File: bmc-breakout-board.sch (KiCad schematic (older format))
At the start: 49 parts, among them J1 PinHeader_2x4, J10 PinHeader_2x4, J11 PinHeader_2x05, J12 61300411121, J13 0473460001, J14 PCIE_BUS_x1, J15 0473460001, J16 PinHeader_1x07, J17 UE27AC54100, J2 PinHeader_2x13, J3 PinHeader_2x08, J4 61300411121, J5 ME1016813401101, J6 61300411121, J7 DC_SOCKET, J8 PinHeader_2x05, J9 PinHeader_1x07, U1 FT234XD-R

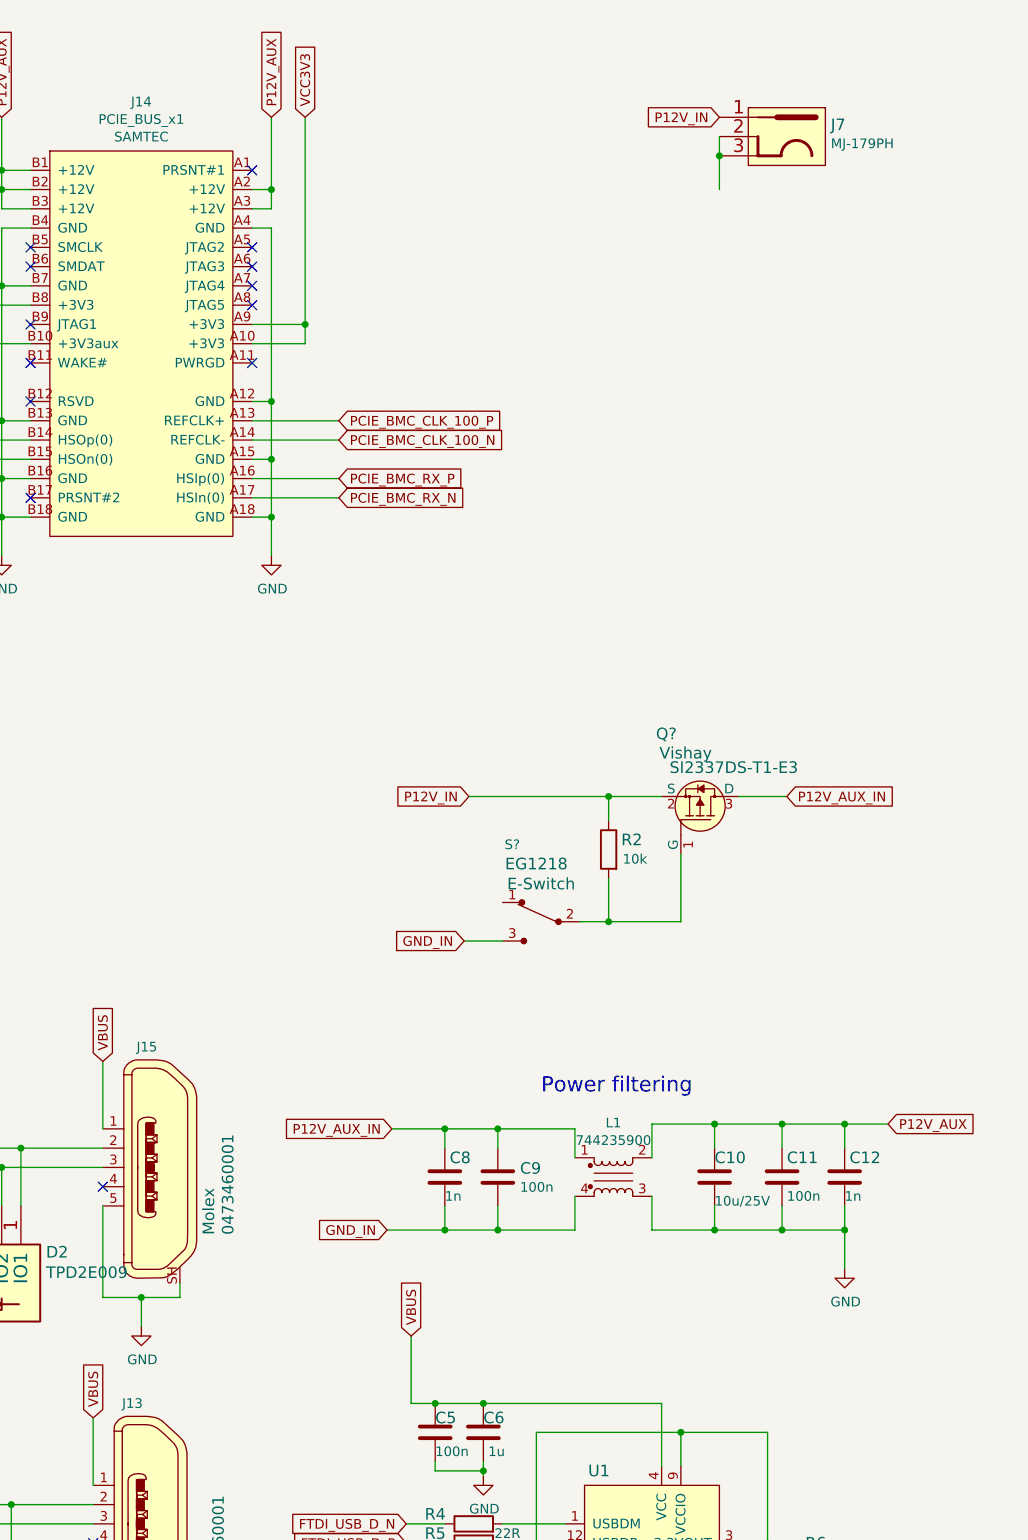
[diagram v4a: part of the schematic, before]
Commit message: Change signal assigment around the power filtering circuit
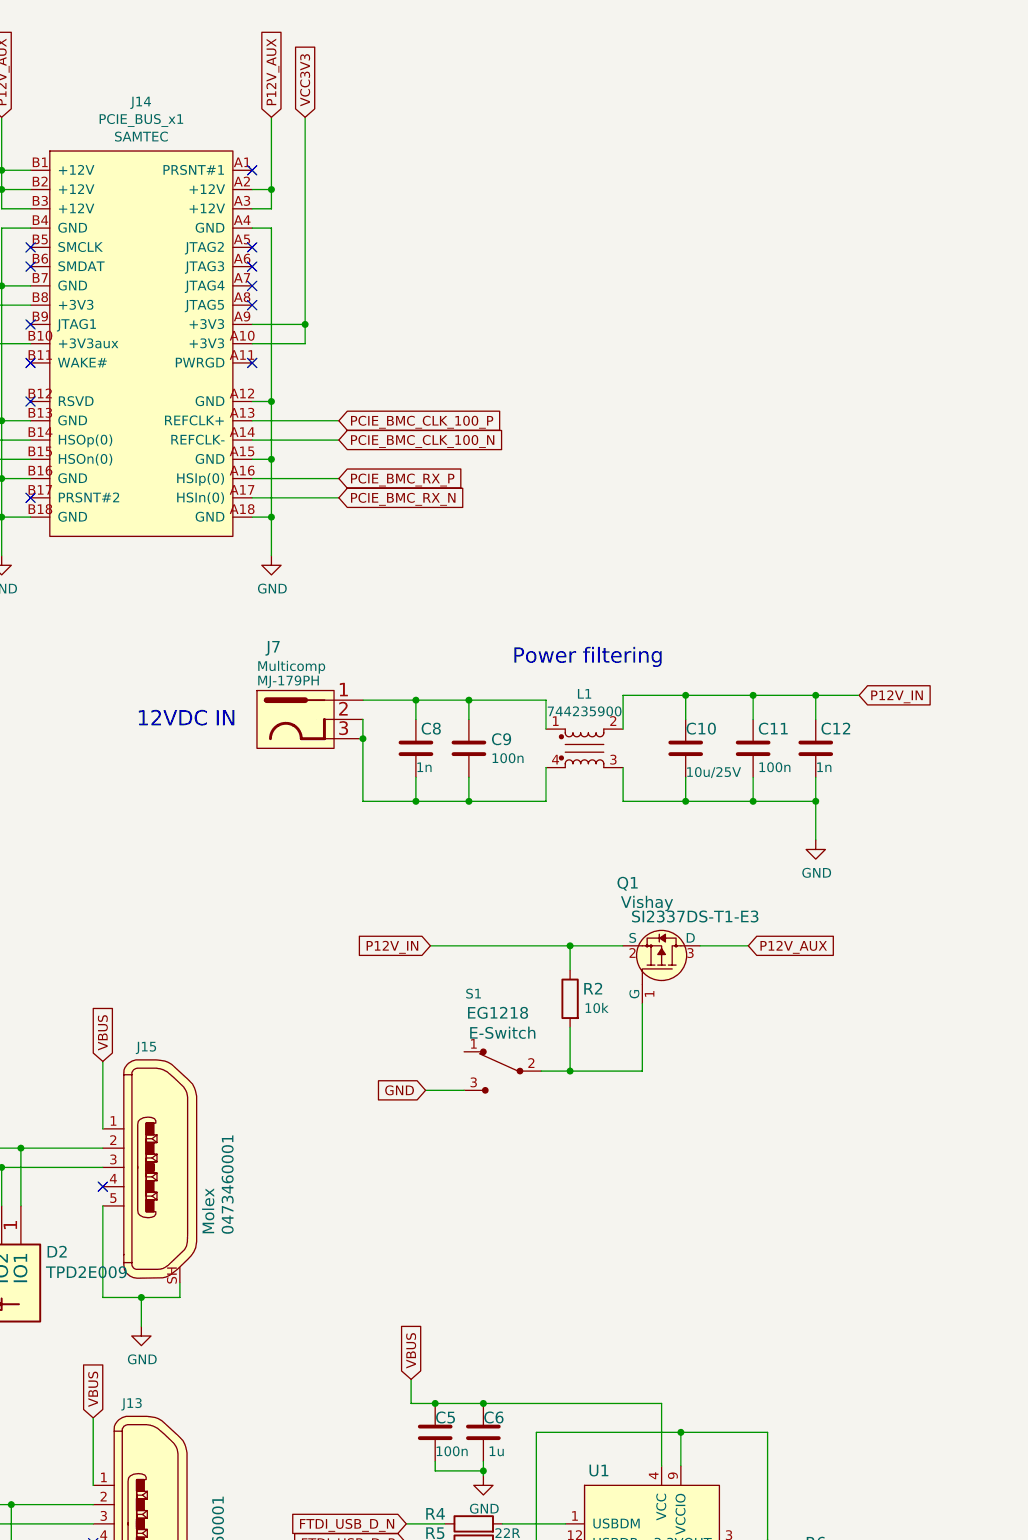
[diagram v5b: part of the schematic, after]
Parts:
- gave numbers to parts that had none: 2
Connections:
- net GND: now also S1.3
- net P12V_AUX: now also Q1.3 (D); no longer C10.1, C11.1, C12.1, L1.2
- net P12V_IN: now also C10.1, C11.1, C12.1, L1.2; no longer J7.1
- net at J7.2, J7.3: now also C8.2, C9.2, L1.4
- removed net GND_IN: C8.2, C9.2, L1.4, S1.3
- net P12V_AUX_IN: no longer names the net of C8.1, C9.1, L1.1
- net P12V_AUX_IN: now also J7.1; no longer Q1.3 (D)
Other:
- note added: "12VDC IN"
- moved on the sheet: C10, C11, C12, C8, C9, J7, L1, Q1, R2, S1

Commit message: Update component arrangement
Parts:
- removed L1: 744235900, bmc-breakout-board-footprints:744235900, symbol bmc-breakout-board:744235900
- added L1: 744235900, antmicro-footprints:744235900, symbol antmicroFixedInductors:744235900
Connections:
- net GND: now also L1.3
- net P12V_IN: now also L1.2
- net at C8.1, C9.1, J7.1: now also L1.1
- net at C8.2, C9.2, J7.2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: now also L1.4
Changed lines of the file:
@@
-$EndComp
-$Comp
-L bmc-breakout-board:744235900 L1
-U 1 1 621486C2
-P 13925 4450
-F 0 "L1" H 13925 4731 50  0000 C CNN
-F 1 "744235900" H 13925 4640 50  0000 C CNN
-F 2 "bmc-breakout-board-footprints:744235900" H 13925 4450 50  0001 C CNN
-F 3 "~" H 13925 4450 50  0001 C CNN
-F 4 "Wurth Elektronik" H 13925 4450 50  0001 C CNN "Manufacturer"
-F 5 "744235900" H 13925 4450 50  0001 C CNN "MPN"
-	1    13925 4450
-	1    0    0    -1
 $EndComp
 $Comp
@@
 Text GLabel 6125 1575 2    50   Input ~ 0
 P12V_AUX
-Text Notes 13550 4025 0    79   ~ 0
+Text Notes 13500 3800 0    79   ~ 0
 Power filtering
 Connection ~ 13325 4725
@@
 Text Notes 11600 4350 0    79   ~ 0
 12VDC IN
+$Comp
+L antmicroFixedInductors:744235900 L1
+U 1 1 614300DC
+P 13925 4450
+F 0 "L1" H 13925 4975 50  0000 C CNN
+F 1 "744235900" H 13925 4275 50  0001 C CNN
+F 2 "antmicro-footprints:744235900" H 14525 4950 50  0001 C CNN
+F 3 "https://www.we-online.de/katalog/datasheet/744235900.pdf" H 13925 4450 50  0001 C CNN
+F 4 "Wurth Elektronik" H 13925 4875 50  0000 C CNN "Manufacturer"
+F 5 "744235900" H 13925 4775 50  0000 C CNN "MPN"
+F 6 "2A" H 14000 5100 50  0001 C CNN "MaxCur"
+F 7 "3.2x4.5" H 14075 5025 50  0001 C CNN "Size"
+F 8 "300n/2A" H 14150 4675 50  0001 C CNN "Val"
+	1    13925 4450
+	1    0    0    -1
+$EndComp
 $EndSCHEMATC

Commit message: Add local lib
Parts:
- L1: footprint antmicro-footprints:744235900 -> bmc-breakout-board-footprints:744235900; symbol antmicroFixedInductors:744235900 -> bmc-breakout-board:744235900
- N2: footprint antmicro-footprints:oshw-logo -> bmc-breakout-board-footprints:oshw-logo; symbol antmicroMechanicalParts:oshw_logo -> bmc-breakout-board:oshw_logo
- Q1: footprint antmicro-footprints:SOT-23-3 -> bmc-breakout-board-footprints:SOT-23-3; symbol antmicroTransistorsFETsMOSFETsSingle:SI2337DS -> bmc-breakout-board:SI2337DS
- S1: footprint antmicro-footprints:Switch_Slide_11.6x4mm_EG1218 -> bmc-breakout-board-footprints:Switch_Slide_11.6x4mm_EG1218; symbol antmicroSlideSwitches:EG1218 -> bmc-breakout-board:EG1218
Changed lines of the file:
@@
 	13050 4725 13325 4725
 $Comp
-L antmicroMechanicalParts:oshw_logo N2
+L bmc-breakout-board:oshw_logo N2
 U 1 1 60C9DEB2
 P 9000 9975
 F 0 "N2" H 9194 9978 50  0000 L CNN
 F 1 "oshw_logo" H 9194 9887 50  0000 L CNN
-F 2 "antmicro-footprints:oshw-logo" H 9020 9735 50  0001 C CNN
+F 2 "bmc-breakout-board-footprints:oshw-logo" H 9020 9735 50  0001 C CNN
 F 3 "" H 9000 9975 50  0001 C CNN
 	1    9000 9975
@@
 	13850 6125 13700 6125
 $Comp
-L antmicroSlideSwitches:EG1218 S1
+L bmc-breakout-board:EG1218 S1
 U 1 1 60FD2969
 P 13500 6125
 F 0 "S1" H 13650 6525 50  0000 C CNN
 F 1 "EG1218" H 13500 6315 50  0001 C CNN
-F 2 "antmicro-footprints:Switch_Slide_11.6x4mm_EG1218" H 13700 6325 50  0001 L CNN
+F 2 "bmc-breakout-board-footprints:Switch_Slide_11.6x4mm_EG1218" H 13700 6325 50  0001 L CNN
 F 3 "http://spec_sheets.e-switch.com/specs/P040040.pdf" H 13700 6425 60  0001 L CNN
 F 4 "EG1218" H 13525 6425 60  0000 C CNN "MPN"
@@
 	13300 6225 13100 6225
 $Comp
-L antmicroTransistorsFETsMOSFETsSingle:SI2337DS Q1
+L bmc-breakout-board:SI2337DS Q1
 U 1 1 612434C1
 P 14325 5475
 F 0 "Q1" V 14650 5300 60  0000 C CNN
 F 1 "SI2337DS" V 14461 5475 60  0001 C CNN
-F 2 "antmicro-footprints:SOT-23-3" H 14525 5675 60  0001 L CNN
+F 2 "bmc-breakout-board-footprints:SOT-23-3" H 14525 5675 60  0001 L CNN
 F 3 "http://www.farnell.com/datasheets/2045706.pdf" H 14525 5775 60  0001 L CNN
 F 4 "SI2337DS-T1-E3" V 14475 5650 60  0000 C CNN "MPN"
@@
 12VDC IN
 $Comp
-L antmicroFixedInductors:744235900 L1
+L bmc-breakout-board:744235900 L1
 U 1 1 614300DC
 P 13925 4450
 F 0 "L1" H 13925 4975 50  0000 C CNN
 F 1 "744235900" H 13925 4275 50  0001 C CNN
-F 2 "antmicro-footprints:744235900" H 14525 4950 50  0001 C CNN
+F 2 "bmc-breakout-board-footprints:744235900" H 14525 4950 50  0001 C CNN
 F 3 "https://www.we-online.de/katalog/datasheet/744235900.pdf" H 13925 4450 50  0001 C CNN
 F 4 "Wurth Elektronik" H 13925 4875 50  0000 C CNN "Manufacturer"

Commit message: Add MPN to the edge connector
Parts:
- J5: MPN (none) -> ME1016813401101; Manufacturer (none) -> Amphenol
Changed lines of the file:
@@
 F 2 "bmc-breakout-board-footprints:ME1016813401101" H 5025 1525 50  0001 C CNN
 F 3 "https://cdn.amphenol-icc.com/media/wysiwyg/files/drawing/cme10168x340x10x.pdf" H 5075 1425 50  0001 C CNN
+F 4 "ME1016813401101" H 4875 1475 50  0001 C CNN "MPN"
+F 5 "Amphenol" H 4875 1475 50  0001 C CNN "Manufacturer"
 	1    4875 1475
 	1    0    0    -1
